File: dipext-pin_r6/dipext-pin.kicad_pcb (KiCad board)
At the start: 2 copper layers, 88.9 x 88.9 mm, 12 parts, among them J1 ZIF, J2 IDC40, J3 Conn_02x20_Odd_Even, J4 Conn_02x20_Odd_Even, J5 01x20, J6 01x20, J7 01x20, J8 01x20

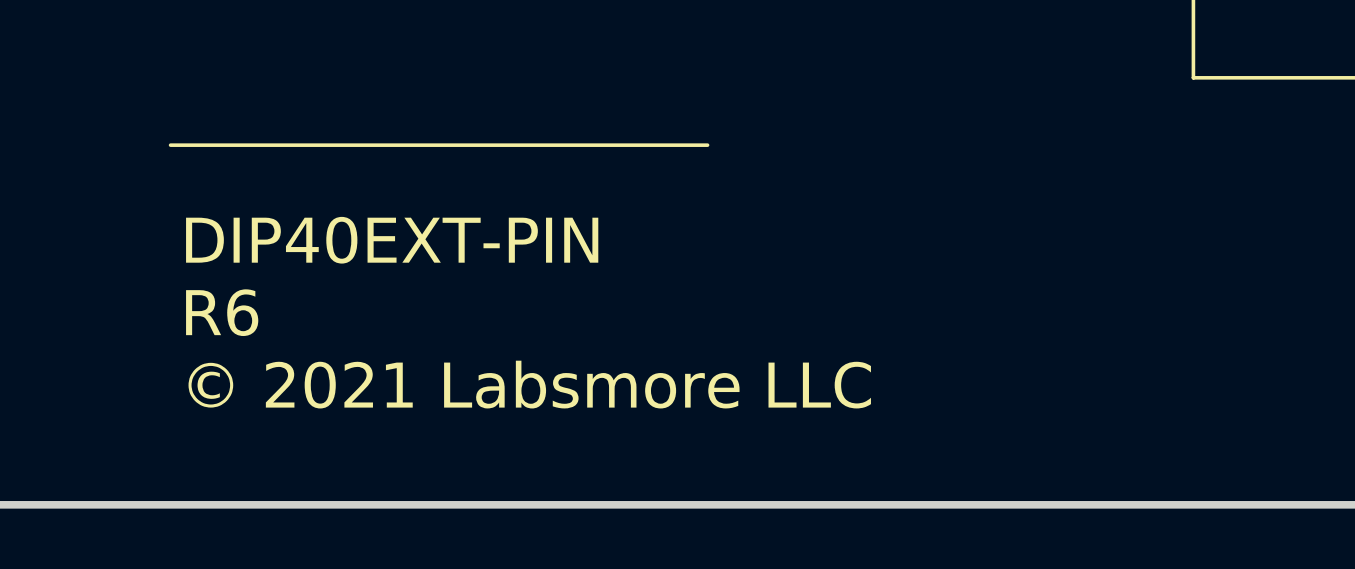
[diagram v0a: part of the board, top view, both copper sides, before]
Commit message: renamve r4 suffix
Signed-off-by: John McMaster <johndmcmaster@gmail.com>
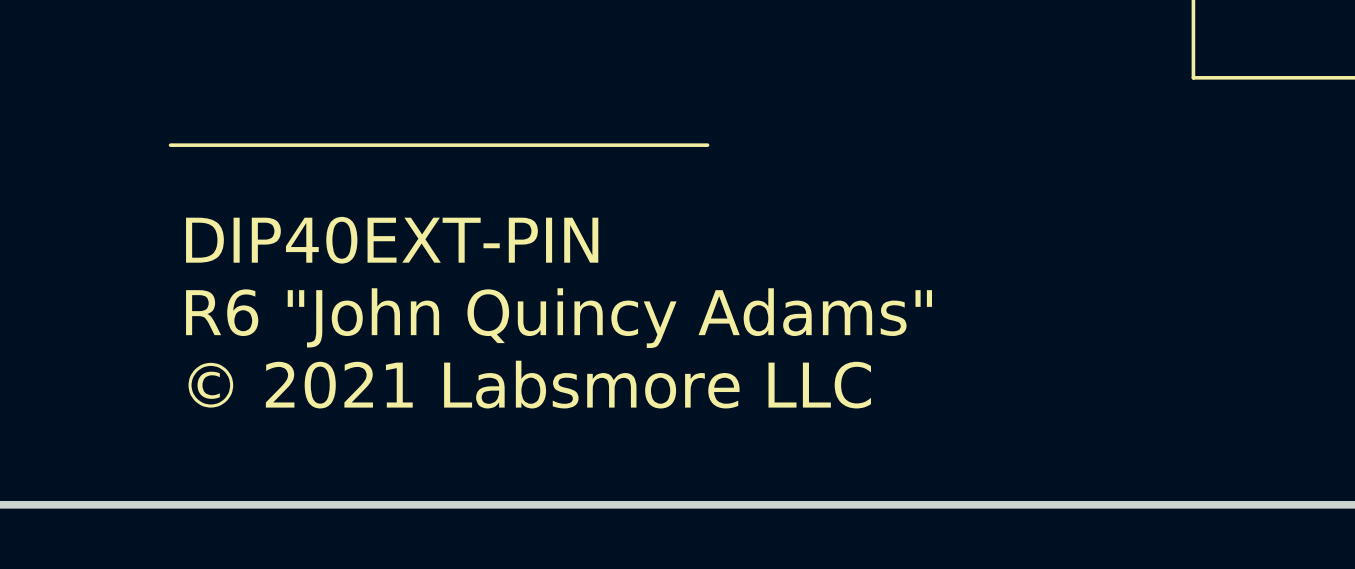
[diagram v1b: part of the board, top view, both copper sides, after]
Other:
- board text added: "DIP40EXT-PIN R6 {dblquote}John Quincy Adams{dblquote} © 2021 Labsmore LLC"
- board text removed: "DIP40EXT-PIN R6 © 2021 Labsmore LLC"
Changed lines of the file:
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@@
   (gr_line (start 25.4 25.4) (end 114.3 25.4) (layer "Edge.Cuts") (width 0.254))
   (gr_line (start 25.4 25.4) (end 25.4 114.3) (layer "Edge.Cuts") (width 0.254))
-  (gr_text "DIP40EXT-PIN\nR6\n© 2021 Labsmore LLC" (at 55.88 107.95) (layer "F.SilkS")
+  (gr_text "DIP40EXT-PIN\nR6 {dblquote}John Quincy Adams{dblquote}\n© 2021 Labsmore LLC" (at 55.88 107.95) (layer "F.SilkS")
     (effects (font (size 1.5 1.5) (thickness 0.3)) (justify left))
   )
